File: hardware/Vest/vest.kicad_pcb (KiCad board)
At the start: 2 copper layers, 152.4 x 101.6 mm, 43 parts, among them P1 USB_B, P2 USB_B, Q1 BC547, Q2 BC547, Q3 BC547

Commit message: Updated pcb
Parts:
- removed Buzzer1: CONN_01X02, Pin_Headers:Pin_Header_Straight_1x02
- removed Buzzer_Tran1, Q1, Q2, Q3, Vib_Tran1: BC547, TO_SOT_Packages_THT:TO-92_Inline_Wide
- removed R17, R22, R23: R, Resistors_SMD:R_1206
- added LF_DATA1: BSS138, TO_SOT_Packages_SMD:SOT-23, F.Cu at (146.1, 99.1)
- added LS_CLK1: BSS138, TO_SOT_Packages_SMD:SOT-23, F.Cu at (147.3, 108.6)
- added Q4: PZT2222A, TO_SOT_Packages_SMD:SOT-23, F.Cu at (73.0, 96.2)
- added Q5: PZT2222A, TO_SOT_Packages_SMD:SOT-23, F.Cu at (131.4, 83.4)
- added R24: 10K, Resistors_SMD:R_1206, F.Cu at (138.4, 99.1)
- added R25: 1K, Resistors_SMD:R_1206, F.Cu at (156.2, 99.1)
- added SP1: SPEAKER, Buzzers_Beepers:MagneticBuzzer_Kingstate_KCG0601, F.Cu at (135.6, 67.0)
- R1, R10, R12, R13, R14, R15, R16: value R -> 0
- R11, R4, R6: value R0 -> 0
- R2: value R -> 10K
- R3, Re1, Re2: value R -> 1K
- R5: value R0 -> R; footprint Resistors_SMD:R_1206 -> Resistors_SMD:R_2010
- Rc2: value R -> 10
- moved R11 106.3 mm to (165.5, 118.1)
- moved R4 76.7 mm to (52.3, 66.8), turned to 90 degrees
- moved R14 76.1 mm to (46.1, 119.4), turned to 180 degrees
- moved R15 67.7 mm to (46.1, 100.6)
- moved R12 66.2 mm to (46.1, 105.1), turned to 180 degrees
- moved R19 53.3 mm to (89.7, 66.8), turned to 0 degrees
- moved R10 53.3 mm to (167.3, 77.7), turned to 180 degrees
- moved R3 34.8 mm to (156.2, 108.6)
- moved R13 34.2 mm to (78.0, 66.8), turned to 90 degrees
- moved R5 33.5 mm to (104.8, 83.8), turned to 0 degrees
- moved R16 31.1 mm to (116.6, 63.2), turned to 270 degrees
- moved R1 30.5 mm to (151.1, 99.1), turned to 90 degrees
- moved R7 29.2 mm to (92.7, 78.7), turned to 180 degrees
- moved Re1 26.1 mm to (82.6, 95.2), turned to 0 degrees
- moved R2 19.8 mm to (140.3, 108.6), turned to 270 degrees
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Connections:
- net RX renamed RX_to_weapon_TX
- net TX renamed TX_to_weapon_RX
- Belt1 pad 4: GND_J -> Net-(Belt1-Pad4)
- IR1 pad 3: GND_J -> Net-(IR1-Pad3)
- LEDs1 pad 1: VCC -> RAW
- LEDs1 pad 2: Net-(LEDs1-Pad2) -> LED_DATA
- LEDs1 pad 3: Net-(LEDs1-Pad3) -> LED_CLK
- Mic1 pad 3: GND_J -> Net-(Mic1-Pad3)
- NRF24L1 pad 1: IRQ -> Net-(NRF24L1-Pad1)
- NRF24L1 pad 2: MISO_OUT -> Net-(NRF24L1-Pad2)
- NRF24L1 pad 3: MOSI -> CE
- NRF24L1 pad 4: SCK -> CSN
- NRF24L1 pad 5: CSN_OUT -> SCK
- NRF24L1 pad 6: CE_OUT -> MOSI
- NRF24L1 pad 7: NRF_VCC_OUT -> MISO
- NRF24L1 pad 8: GND_OUT -> Net-(NRF24L1-Pad8)
- R1 pad 1: Net-(Q1-Pad2) -> VCC
- R1 pad 2: A0 -> VCC
- R10 pad 1: Net-(R10-Pad1) -> GND
- R10 pad 2: GND_OUT -> GND
- R11 pad 1: GND_J -> Net-(LEDs1-Pad4)
- R11 pad 2: Net-(R11-Pad2) -> GND
- R12 pad 1: GND_J -> Net-(IR1-Pad3)
- R12 pad 2: Net-(R10-Pad1) -> GND
- R13 pad 2: Net-(R13-Pad2) -> GND
- R14 pad 1: MISO -> Net-(Belt1-Pad4)
- R14 pad 2: Net-(R14-Pad2) -> GND
- R15 pad 1: Net-(R15-Pad1) -> GND
- R15 pad 2: CE_OUT -> Net-(Q4-Pad3)
- R16 pad 1: CSN -> GND
- R16 pad 2: Net-(R13-Pad1) -> Net-(Q5-Pad3)
- R2 pad 1: Net-(Q2-Pad2) -> VCC
- R3 pad 1: Net-(Q3-Pad2) -> RAW
- R3 pad 2: A2 -> LED_CLK
- R4 pad 1: Net-(R11-Pad2) -> Net-(Mic1-Pad3)
- R5 pad 1: GND -> IRQ
- R5 pad 2: GND_J2 -> Net-(NRF24L1-Pad8)
- R6 pad 1: Net-(Q3-Pad3) -> VCC
- R6 pad 2: GND_J2 -> VCC
- R7 pad 1: Net-(R14-Pad2) -> Net-(NRF24L1-Pad1)
- R7 pad 2: MISO_OUT -> Net-(R13-Pad1)
- R9 pad 1: Net-(R13-Pad2) -> VCC
- R9 pad 2: CSN_OUT -> Net-(NRF24L1-Pad2)
- Re1 pad 2: GND_J -> PIN6
- Re2 pad 1: GND -> PIN10_OUT
- uP1 pad 20: GND -> Net-(uP1-Pad20)
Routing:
- net GND: track 236.1 -> 451.1 mm
- net GND_J: track 156.8 -> 0.00 mm
- net VCC_J: track 236.1 -> 118.6 mm
- net VCC: track 100.2 -> 160.1 mm
- net MISO_OUT: track 55.1 -> 0.00 mm
- net SCK: track 54.7 -> 23.2 mm
- net A1: track 10.8 -> 40.3 mm
- net Net-(Q4-Pad3): track 0.00 -> 28.3 mm
- net Net-(Q5-Pad3): track 0.00 -> 28.1 mm
- net CSN: track 8.33 -> 35.4 mm
- net PIN6: track 36.0 -> 11.0 mm
- net A0: track 11.3 -> 36.1 mm
- net LED_DATA: track 0.00 -> 21.3 mm
- net RAW: track 128.2 -> 147.7 mm
- net LED_CLK: track 0.00 -> 19.4 mm
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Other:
- outline, holes or cut-outs redrawn

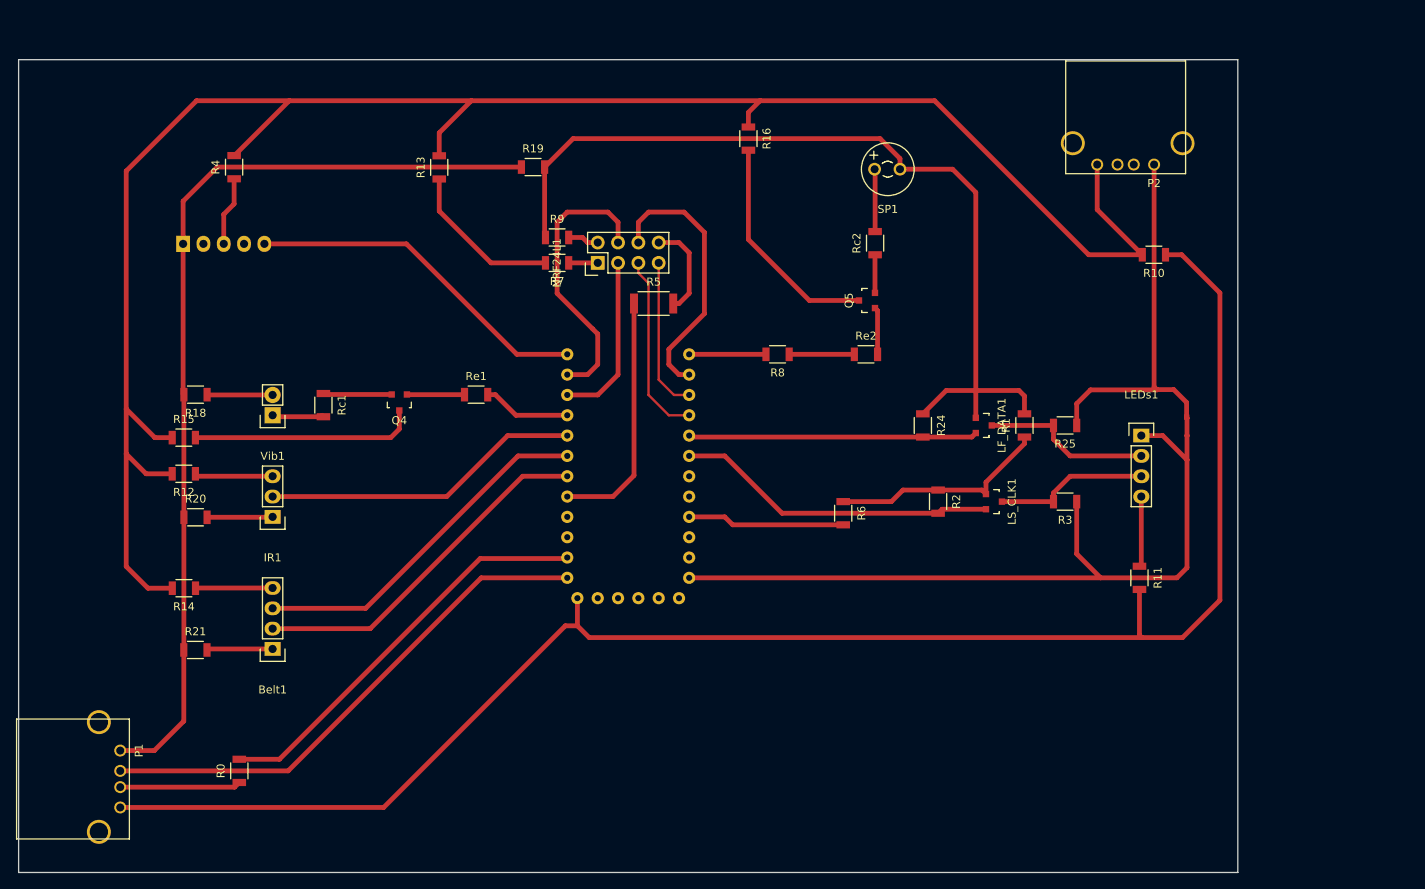
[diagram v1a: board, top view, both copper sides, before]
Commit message: updated pcb: change track passing through 1206 from 0.6 to 0.3
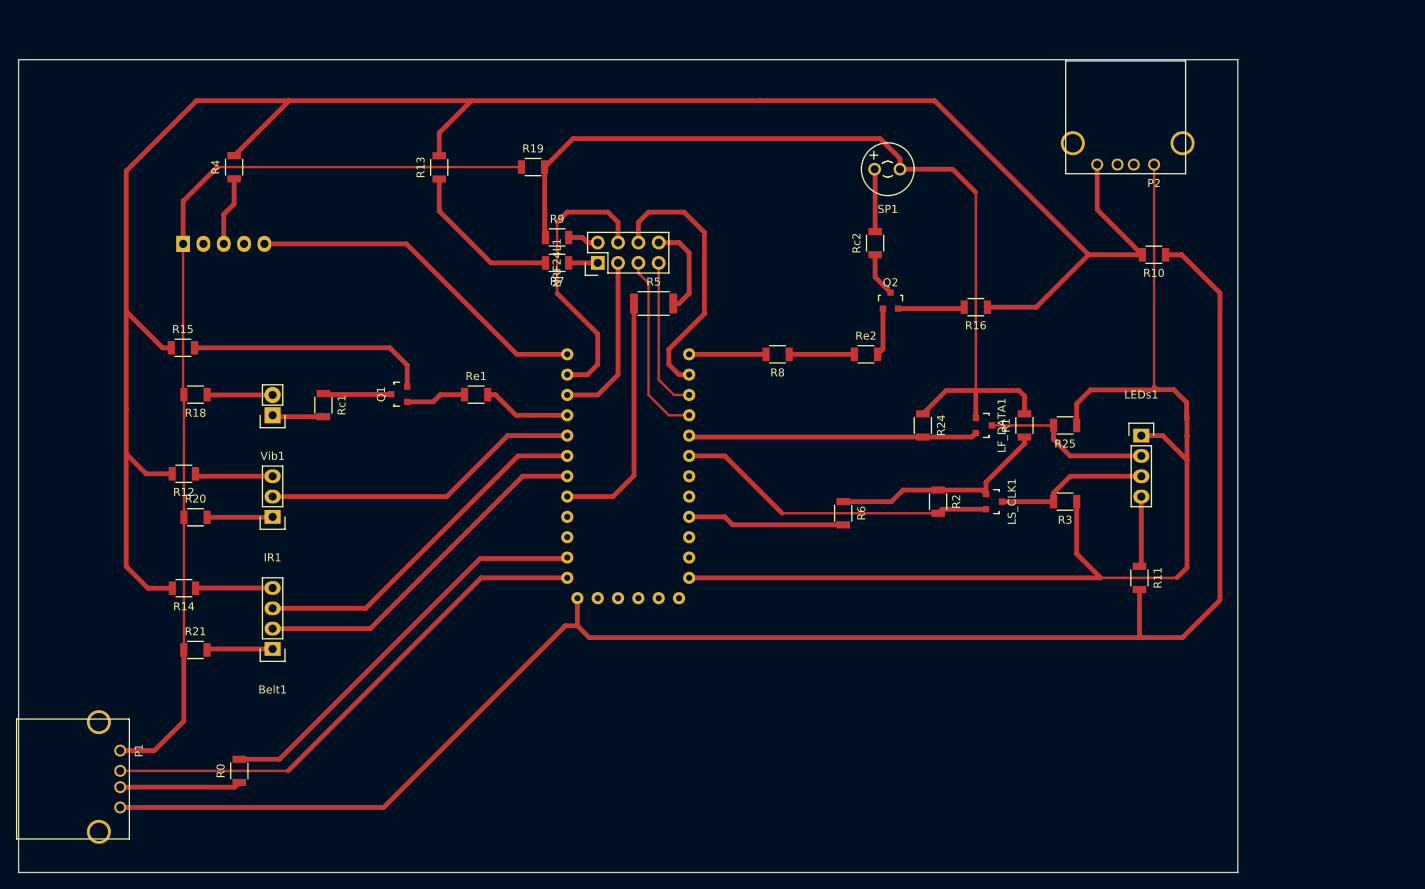
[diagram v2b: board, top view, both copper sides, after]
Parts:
- removed Q4, Q5: PZT2222A, TO_SOT_Packages_SMD:SOT-23
- added Q1: MMBT3904, TO_SOT_Packages_SMD:SOT-23, F.Cu at (73.0, 95.2)
- added Q2: MMBT3904, TO_SOT_Packages_SMD:SOT-23, F.Cu at (134.4, 83.5)
- moved R16 35.4 mm to (145.0, 84.3), turned to 180 degrees
- moved R15 11.2 mm to (45.9, 89.4)
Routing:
- net Net-(Q2-Pad2): track 28.1 -> 8.43 mm
- net GND: track 451.1 -> 462.9 mm
- net Net-(Q1-Pad2): track 28.3 -> 30.2 mm
- net Net-(Q2-Pad3): track 4.77 -> 5.55 mm
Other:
- net class small added: clearance 0.8, trace_width 0.3, via_dia 0.6, via_drill 0.4

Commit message: Added 2 more connectors
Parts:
- added LEDs2: CONN_01X04, Pin_Headers:Pin_Header_Straight_1x04, F.Cu at (99.3, 71.5)
- added LEDs3: CONN_01X04, Pin_Headers:Pin_Header_Straight_1x04, F.Cu at (119.7, 140.4)
- added R17: 0, Resistors_SMD:R_1206, F.Cu at (162.7, 109.0)
- added R23: 0, Resistors_SMD:R_1206, F.Cu at (144.9, 90.8)
- added R26: 0, Resistors_SMD:R_1206, F.Cu at (111.4, 65.8)
- added R27: 0, Resistors_SMD:R_1206, F.Cu at (122.3, 125.6)
- moved R19 14.7 mm to (104.2, 64.4), turned to 270 degrees
- moved LEDs1 6.40 mm to (160.4, 103.8), turned to 90 degrees
- moved R3 1.94 mm to (156.2, 110.5)
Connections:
- LEDs1 pad 1: RAW -> Net-(LEDs1-Pad1)
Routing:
- net Net-(LEDs2-Pad1): track 0.00 -> 65.8 mm
- net GND: track 462.9 -> 508.4 mm
- net VCC_J: track 118.6 -> 140.4 mm
- net Net-(LEDs2-Pad4): track 0.00 -> 18.4 mm
- net RAW: track 147.7 -> 166.0 mm
- net Net-(LEDs3-Pad1): track 0.00 -> 14.4 mm
- net VCC: track 160.1 -> 168.5 mm
- net Net-(LEDs1-Pad4): track 8.80 -> 14.2 mm
- net Net-(LEDs1-Pad1): track 0.00 -> 5.28 mm
- net LED_CLK: track 19.4 -> 24.6 mm
- net LED_DATA: track 21.3 -> 19.7 mm

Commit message: Updated pcb
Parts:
- P2: value USB_B -> USB_B_Power; footprint Connect:USB_A -> Connect:USB_B
- moved P1 36.7 mm to (73.7, 130.8)
- moved R0 33.4 mm to (85.2, 133.3)
- moved R21 30.2 mm to (77.0, 120.7)
- moved R14 30.0 mm to (75.3, 113.0)
- moved Belt1 27.8 mm to (84.2, 120.5)
- moved R15 24.4 mm to (70.1, 86.1)
- moved Mic1 24.2 mm to (70.1, 76.5)
- moved R20 23.8 mm to (71.0, 106.7)
- moved R4 23.6 mm to (75.9, 66.8)
- moved R12 22.5 mm to (68.3, 101.5)
- moved IR1 21.4 mm to (78.2, 106.6)
- moved R18 19.8 mm to (67.3, 94.1)
- moved Vib1 16.2 mm to (73.3, 96.8)
- moved Rc1 14.7 mm to (78.1, 95.4)
- moved Q1 9.88 mm to (82.8, 93.8)
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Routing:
- net GND: track 508.4 -> 410.5 mm
- net TX_to_weapon_RX: track 65.9 -> 31.8 mm
- net RX_to_weapon_TX: track 51.4 -> 21.2 mm
- net VCC_J: track 140.4 -> 111.2 mm
- net PIN4: track 44.7 -> 17.3 mm
- net PIN3: track 44.7 -> 17.5 mm
- net PIN5: track 40.0 -> 17.3 mm
- net PIN9: track 43.6 -> 21.2 mm
- net Net-(Q1-Pad2): track 30.2 -> 16.4 mm
- net PIN6: track 11.0 -> 5.50 mm
- net Net-(Q1-Pad3): track 8.59 -> 3.71 mm
- net Net-(R13-Pad1): track 20.0 -> 15.2 mm
- net Net-(P1-Pad3): track 15.1 -> 11.8 mm
- net Vib_VCC_OUT: track 8.21 -> 5.19 mm
- net Net-(Q1-Pad1): track 7.54 -> 4.79 mm
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
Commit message: updated pcb
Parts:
- removed R0: R0, Resistors_SMD:R_1206
- removed R13, R26: 0, Resistors_SMD:R_1206
- removed R19, R20, R21: R, Resistors_SMD:R_1206
- added R22: 0, Resistors_SMD:R_1206, F.Cu at (95.8, 113.2)
- Belt1, IR1, LEDs1, LEDs2, NRF24L1, P1, P2, Vib1: moved to B.Cu
- R18, R7: footprint Resistors_SMD:R_1206 -> Resistors_SMD:R_2010
- R5: footprint Resistors_SMD:R_2010 -> Resistors_SMD:R_1206
- R8: footprint Resistors_SMD:R_1206 -> Resistors_SMD:R_2512
- SP1: footprint Buzzers_Beepers:MagneticBuzzer_Kingstate_KCG0601 -> Buzzers_Beepers:MagneticBuzzer_ProSignal_ABI-010-RC; moved to B.Cu
- moved R18 51.0 mm to (115.7, 77.9), turned to 0 degrees
- moved LEDs2 44.8 mm to (143.2, 62.5), turned to 5 degrees
- moved R9 40.1 mm to (132.7, 77.6)
- moved R7 36.1 mm to (128.5, 83.0)
- moved SP1 31.2 mm to (166.3, 61.4)
- moved NRF24L1 27.6 mm to (124.2, 70.6), turned to 270 degrees
- moved R23 27.0 mm to (171.3, 85.1)
- moved Belt1 27.0 mm to (110.6, 114.8), turned to 0 degrees
- moved LEDs1 26.9 mm to (186.7, 98.1), turned to 270 degrees
- moved LS_CLK1 26.9 mm to (173.6, 102.9)
- moved R1 26.9 mm to (177.4, 93.3)
- moved R16 26.9 mm to (171.3, 78.6)
- moved R17 26.9 mm to (189.0, 103.3)
- moved R6 26.9 mm to (154.8, 104.3)
- moved IR1 26.9 mm to (104.5, 100.9), turned to 0 degrees
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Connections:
- Belt1 pad 1: Belt_VCC_OUT -> VCC
- IR1 pad 1: Buzzer_VCC_OUT -> VCC
- LEDs2 pad 4: Net-(LEDs2-Pad4) -> GND
- Mic1 pad 1: VCC_J -> VCC
- NRF24L1 pad 1: Net-(NRF24L1-Pad1) -> GND
- NRF24L1 pad 2: Net-(NRF24L1-Pad2) -> VCC
- NRF24L1 pad 8: Net-(NRF24L1-Pad8) -> IRQ
- P1 pad 1: VCC_J -> Net-(P1-Pad1)
- P1 pad 3: Net-(P1-Pad3) -> RX_to_weapon_TX
- R18 pad 1: Vib_VCC_OUT -> VCC
- R18 pad 2: VCC_J -> VCC
- R5 pad 1: IRQ -> Net-(R5-Pad1)
- R5 pad 2: Net-(NRF24L1-Pad8) -> CE
- R7 pad 1: Net-(NRF24L1-Pad1) -> VCC
- R7 pad 2: Net-(R13-Pad1) -> VCC
- R9 pad 1: VCC -> MOSI
- R9 pad 2: Net-(NRF24L1-Pad2) -> Net-(R9-Pad2)
- Vib1 pad 2: Vib_VCC_OUT -> VCC
- uP1 pad 16: CE -> CSN
- uP1 pad 17: CSN -> Net-(R5-Pad1)
- uP1 pad 29: MOSI -> Net-(R9-Pad2)
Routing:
- net VCC_J: track 111.2 -> 0.00 mm
- net VCC: track 168.5 -> 233.7 mm
- net Net-(P1-Pad1): track 0.00 -> 48.9 mm
- net MOSI: track 33.8 -> 5.67 mm
- net SCK: track 23.2 -> 47.7 mm
- net Net-(R5-Pad1): track 0.00 -> 22.4 mm
- net Net-(LEDs2-Pad4): track 18.4 -> 0.00 mm
- net MISO: track 19.2 -> 35.4 mm
- net Net-(R9-Pad2): track 0.00 -> 15.6 mm
- net Net-(R13-Pad1): track 15.2 -> 0.00 mm
- net CSN: track 35.4 -> 22.6 mm
- net Net-(LEDs3-Pad1): track 14.4 -> 27.0 mm
- net Net-(LEDs2-Pad1): track 65.8 -> 53.7 mm
- net Net-(NRF24L1-Pad8): track 11.9 -> 0.00 mm
- net Net-(P1-Pad3): track 11.8 -> 0.00 mm
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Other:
- board size 152.4 x 101.6 mm -> 114.8 x 96.6 mm
